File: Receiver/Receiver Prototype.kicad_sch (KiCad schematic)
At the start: 108 parts, among them J1 Conn_01x02_Socket, J10 Conn_01x01, J11 Conn_Coaxial, J12 Conn_Coaxial, J13 Conn_Coaxial, J14 Conn_Coaxial, J15 Conn_01x01, J16 Conn_01x01, J17 Conn_01x02, J18 Conn_01x02, J19 Conn_01x01, J2 Conn_01x01, J20 Conn_01x01, J21 Conn_01x01, J22 Conn_01x01, J23 Conn_01x02, J24 Conn_01x02, J25 Conn_01x01, J26 Conn_01x03, J27 Conn_01x03, J28 Conn_01x02, J29 Conn_01x03, J3 Conn_01x01, J30 Conn_01x03, J4 Conn_Coaxial, J5 Conn_01x01, J6 Conn_01x02, J7 Conn_Coaxial, J8 Conn_Coaxial, J9 Conn_01x01, U1 OPA3692ID, U2 AD8692ARZ, U3 OPA692IDBVR, U4 LT3045EMSE-PBF, U5 AD607ARSZ, U6 LT3094EMSE-PBF

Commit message: Changed the AD8692 and SMD diodes footprints
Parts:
- D5, D6: footprint 1N4148WS-HE3-18:CR_HE3-18_VIS -> Diode_SMD:D_0805_2012Metric_Pad1.15x1.40mm_HandSolder
- U2: footprint AD8692:R-8_ADI -> AD8692:SOIC127P600X175-8N
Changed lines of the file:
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@@
 			)
 		)
-		(property "Footprint" "1N4148WS-HE3-18:CR_HE3-18_VIS"
+		(property "Footprint" "Diode_SMD:D_0805_2012Metric_Pad1.15x1.40mm_HandSolder"
 			(at 335.28 213.36 0)
 			(effects
@@
 			)
 		)
-		(property "Footprint" "1N4148WS-HE3-18:CR_HE3-18_VIS"
+		(property "Footprint" "Diode_SMD:D_0805_2012Metric_Pad1.15x1.40mm_HandSolder"
 			(at 322.58 213.36 0)
 			(effects
@@
 			)
 		)
-		(property "Footprint" "AD8692:R-8_ADI"
+		(property "Footprint" "AD8692:SOIC127P600X175-8N"
 			(at 97.79 177.8 0)
 			(effects

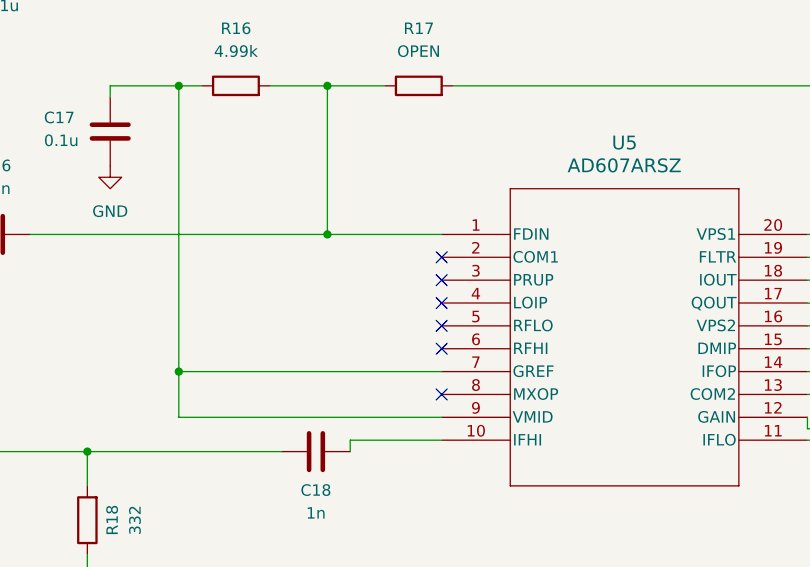
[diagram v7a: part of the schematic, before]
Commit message: Connected COM1 to Ground in AD607
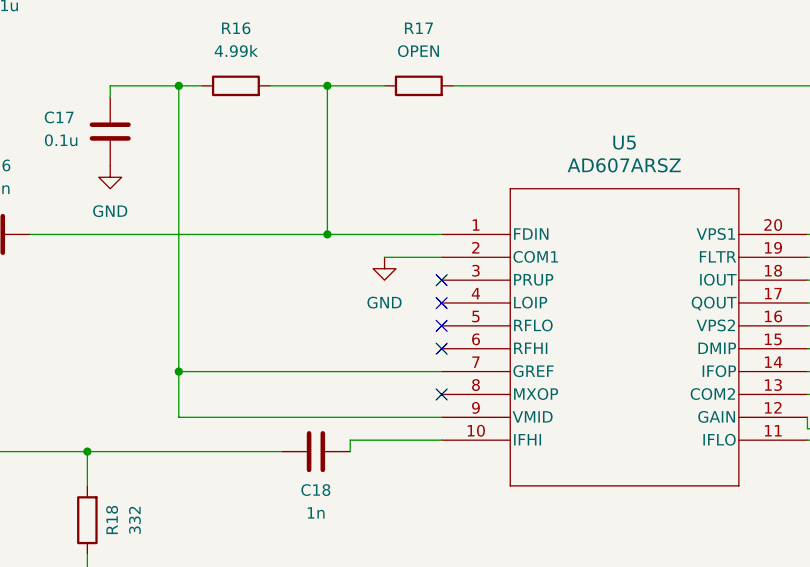
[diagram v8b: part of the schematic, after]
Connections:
- net GND: now also U5.2 (COM1)
- no-connect marks 14 -> 13
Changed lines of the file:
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@@
 		(at 444.5 321.31)
 	)
-	(no_connect
-		(at 444.5 311.15)
-	)
 	(wire
 		(pts
@@
 	(wire
 		(pts
+			(xy 438.15 311.15) (xy 444.5 311.15)
+		)
+		(stroke
+			(width 0)
+			(type default)
+		)
+	)
+	(wire
+		(pts
 			(xy 534.67 308.61) (xy 534.67 311.15)
 		)
@@
 					(unit 1)
 				)
+			)
+		)
+	)
+	(symbol
+		(lib_id "power:GND")
+		(at 438.15 311.15 0)
+		(unit 1)
+		(exclude_from_sim no)
+		(in_bom yes)
+		(on_board yes)
+		(dnp no)
+		(fields_autoplaced yes)
+		(property "Reference" "#PWR038"
+			(at 438.15 317.5 0)
+			(effects
+				(font
+					(size 1.27 1.27)
+				)
+				(hide yes)
+			)
+		)
+		(property "Value" "GND"
+			(at 438.15 316.23 0)
+			(effects
+				(font
+					(size 1.27 1.27)
+				)
+			)
+		)
+		(property "Footprint" ""
+			(at 438.15 311.15 0)
+			(effects
+				(font
+					(size 1.27 1.27)
+				)
+				(hide yes)
+			)
+		)
+		(property "Datasheet" ""
+			(at 438.15 311.15 0)
+			(effects
+				(font
+					(size 1.27 1.27)
+				)
+				(hide yes)
+			)
+		)
+		(property "Description" "Power symbol creates a global label with name \"GND\" , ground"
+			(at 438.15 311.15 0)
+			(effects
+				(font
+					(size 1.27 1.27)
+				)
+				(hide yes)
+			)
+		)
+		(pin "1"
+		)
+		(instances
+			(project "Receiver Prototype"
+				(path "/3aa39536-321e-46e0-967e-be2d644a910c"
+					(reference "#PWR038")
+					(unit 1)
+				)
